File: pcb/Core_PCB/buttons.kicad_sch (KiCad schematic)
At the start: 22 parts, among them J2 Conn_01x08, J8 Conn_01x02_MountingPin, Q1 BSN20, U2 MPR121_BREAKOUT

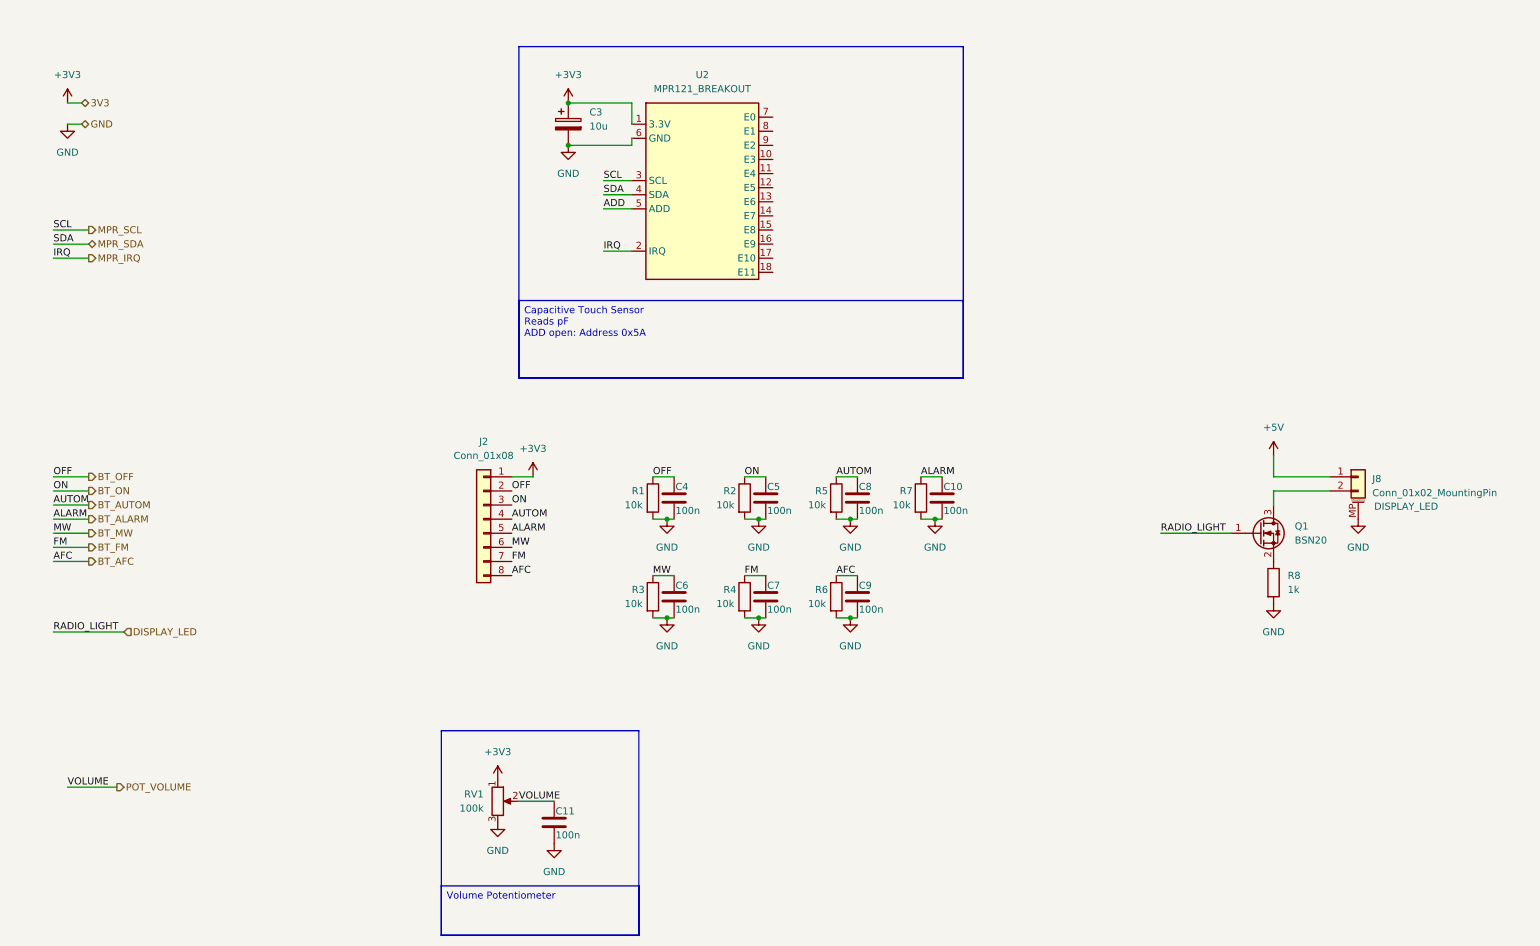
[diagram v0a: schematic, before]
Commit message: SCH: audio gain control via mux (HEF4051), buttons read via i2c io expander (MCP23017)
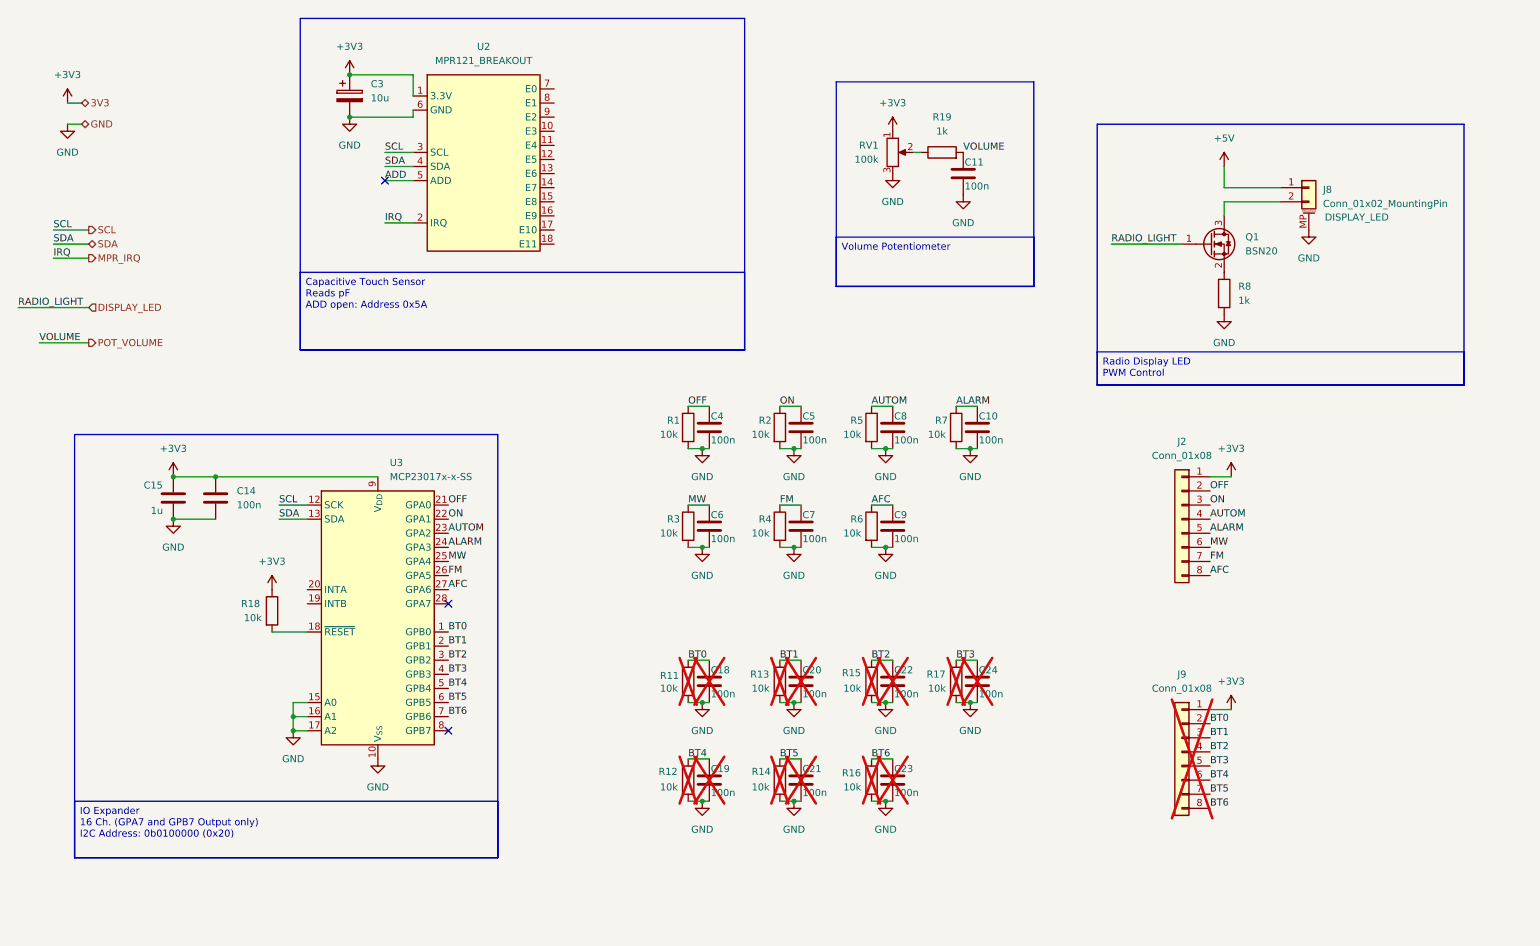
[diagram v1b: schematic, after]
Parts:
- added C14: 100n, symbol Device:C
- added C15: 1u, symbol Device:C
- added C18, C19, C20, C21, C22, C23, C24: 100n, Capacitor_SMD:C_0603_1608Metric_Pad1.08x0.95mm_HandSolder, symbol Device:C
- added J9: Conn_01x08, symbol Connector_Generic:Conn_01x08
- added R11, R12, R13, R14, R15, R16, R17, R18: 10k, Resistor_SMD:R_0603_1608Metric_Pad0.98x0.95mm_HandSolder, symbol Device:R
- added R19: 1k, symbol Device:R
- added U3: MCP23017x-x-SS, Package_SO:SSOP-28_5.3x10.2mm_P0.65mm, symbol Interface_Expansion:MCP23017x-x-SS
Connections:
- net +3V3: now also C14.1, C15.1, J9.1 (Pin_1), R18.1, U3.9 (V_{DD})
- net GND: now also C14.2, C15.2, C18.2, C19.2, C20.2, C21.2, C22.2, C23.2, C24.2, R11.2, R12.2, R13.2, R14.2, R15.2, R16.2, R17.2, U3.10 (V_{SS}), U3.15 (A0), U3.16 (A1), U3.17 (A2)
- net POT_VOLUME: now also R19.2; no longer RV1.2
- net BT_AFC renamed AFC
- net AFC: now also U3.27 (GPA6)
- net BT_ALARM renamed ALARM
- net ALARM: now also U3.24 (GPA3)
- net BT_AUTOM renamed AUTOM
- net AUTOM: now also U3.23 (GPA2)
- net BT_FM renamed FM
- net FM: now also U3.26 (GPA5)
- net BT_MW renamed MW
- net MW: now also U3.25 (GPA4)
- net BT_OFF renamed OFF
- net OFF: now also U3.21 (GPA0)
- net BT_ON renamed ON
- net ON: now also U3.22 (GPA1)
- net MPR_SCL renamed SCL
- net SCL: now also U3.12 (SCK)
- net MPR_SDA renamed SDA
- net SDA: now also U3.13 (SDA)
- new net: R19.1, RV1.2
- new net: R18.2, U3.18 (~{RESET})
- new net BT0: C18.1, J9.2 (Pin_2), R11.1, U3.1 (GPB0)
- new net BT1: C20.1, J9.3 (Pin_3), R13.1, U3.2 (GPB1)
- new net BT2: C22.1, J9.4 (Pin_4), R15.1, U3.3 (GPB2)
- new net BT3: C24.1, J9.5 (Pin_5), R17.1, U3.4 (GPB3)
- new net BT4: C19.1, J9.6 (Pin_6), R12.1, U3.5 (GPB4)
- new net BT5: C21.1, J9.7 (Pin_7), R14.1, U3.6 (GPB5)
- new net BT6: C23.1, J9.8 (Pin_8), R16.1, U3.7 (GPB6)
- no-connect marks 0 -> 3
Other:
- moved on the sheet: C10, C3, C4, C5, C6, C7, C8, C9, J2, J8, Q1, R1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

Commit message: SCH: annotated sheets, reannotated all components
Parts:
- RV1: Name (none) -> VOLUME
- renumbered C5 to C10, C8 to C11, C10 to C12, C15 to C13, C6 to C15, C7 to C16, C9 to C17, C20 to C19, C22 to C20, C24 to C21, C19 to C22, C21 to C23, C23 to C24, C3 to C7, C11 to C8, C4 to C9, J8 to J7, J2 to J8, R4 to R10, R6 to R11, R18 to R12, R11 to R13, R13 to R14, R17 to R16, R12 to R17, R14 to R18, R16 to R19, R19 to R3, R8 to R4, R1 to R5, R2 to R6, R5 to R7, R7 to R8, R3 to R9, U2 to U3, U3 to U4
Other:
- company: (none) -> brunolalb@gmail.com
- title: (none) -> Alarm Clock Resto Mod - Core PCB

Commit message: SCH: assigned footprints to what had missing, replaced some polarized caps with non polarized, added connector for capacitance sensor, ran electric test and fixed minor issues
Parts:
- added J10: Conn_01x12, Connector_PinSocket_2.54mm:PinSocket_1x12_P2.54mm_Vertical, symbol Connector_Generic:Conn_01x12
- C13: footprint (none) -> Capacitor_SMD:C_0805_2012Metric_Pad1.18x1.45mm_HandSolder
- C14: footprint (none) -> Capacitor_SMD:C_0603_1608Metric_Pad1.08x0.95mm_HandSolder
- C7: footprint (none) -> Capacitor_SMD:C_0805_2012Metric_Pad1.18x1.45mm_HandSolder; symbol Device:C_Polarized -> Device:C
- J7: footprint (none) -> RadioWecker:JST_S2B-XH-SM4-TB
- J8, J9: footprint (none) -> Connector_PinSocket_2.54mm:PinSocket_1x08_P2.54mm_Vertical
- R3, R4, RV1: footprint (none) -> Resistor_SMD:R_0603_1608Metric_Pad0.98x0.95mm_HandSolder
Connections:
- net at U3.10 (E3): now also J10.4 (Pin_4)
- net at U3.11 (E4): now also J10.5 (Pin_5)
- net at U3.12 (E5): now also J10.6 (Pin_6)
- net at U3.13 (E6): now also J10.7 (Pin_7)
- net at U3.14 (E7): now also J10.8 (Pin_8)
- net at U3.15 (E8): now also J10.9 (Pin_9)
- net at U3.16 (E9): now also J10.10 (Pin_10)
- net at U3.17 (E10): now also J10.11 (Pin_11)
- net at U3.18 (E11): now also J10.12 (Pin_12)
- net at U3.7 (E0): now also J10.1 (Pin_1)
- net at U3.8 (E1): now also J10.2 (Pin_2)
- net at U3.9 (E2): now also J10.3 (Pin_3)
- net POT_VOLUME renamed VOLUME_POT
- no-connect marks 3 -> 5

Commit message: SCH - audio: screw terminal was facing the wrong direction; buttons: volume pot had wrong footprint, added +5V input; processor: use alternative arduino symbol and custom footprint (with 3d model), added reset switch, adjusted rule for PWR lines
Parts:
- RV1: footprint Resistor_SMD:R_0603_1608Metric_Pad0.98x0.95mm_HandSolder -> Connector_PinSocket_2.54mm:PinSocket_1x03_P2.54mm_Vertical
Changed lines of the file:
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@@
+	(wire
+		(pts
+			(xy 30.48 24.13) (xy 33.02 24.13)
+		)
+		(stroke
+			(width 0)
+			(type default)
+		)
+	)
 	(wire
 		(pts
@@
 			)
 			(justify left bottom)
+		)
+	)
+	(hierarchical_label "+5V"
+		(shape bidirectional)
+		(at 33.02 24.13 0)
+		(effects
+			(font
+				(size 1.27 1.27)
+			)
+			(justify left)
 		)
 	)
@@
 			)
 		)
-		(property "Footprint" "Resistor_SMD:R_0603_1608Metric_Pad0.98x0.95mm_HandSolder"
+		(property "Footprint" "Connector_PinSocket_2.54mm:PinSocket_1x03_P2.54mm_Vertical"
 			(at 179.07 43.18 0)
 			(hide yes)
@@
 					(unit 1)
 				)
+			)
+		)
+	)
+	(symbol
+		(lib_id "power:+5V")
+		(at 30.48 24.13 0)
+		(unit 1)
+		(body_style 1)
+		(exclude_from_sim no)
+		(in_bom yes)
+		(on_board yes)
+		(in_pos_files yes)
+		(dnp no)
+		(fields_autoplaced yes)
+		(property "Reference" "#PWR068"
+			(at 30.48 27.94 0)
+			(hide yes)
+			(show_name no)
+			(do_not_autoplace no)
+			(effects
+				(font
+					(size 1.27 1.27)
+				)
+			)
+		)
+		(property "Value" "+5V"
+			(at 30.48 19.05 0)
+			(show_name no)
+			(do_not_autoplace no)
+			(effects
+				(font
+					(size 1.27 1.27)
+				)
+			)
+		)
+		(property "Footprint" ""
+			(at 30.48 24.13 0)
+			(hide yes)
+			(show_name no)
+			(do_not_autoplace no)
+			(effects
+				(font
+					(size 1.27 1.27)
+				)
+			)
+		)
+		(property "Datasheet" ""
+			(at 30.48 24.13 0)
+			(hide yes)
+			(show_name no)
+			(do_not_autoplace no)
+			(effects
+				(font
+					(size 1.27 1.27)
+				)
+			)
+		)
+		(property "Description" "Power symbol creates a global label with name \"+5V\""
+			(at 30.48 24.13 0)
+			(hide yes)
+			(show_name no)
+			(do_not_autoplace no)
+			(effects
+				(font
+					(size 1.27 1.27)
+				)
+			)
+		)
+		(pin "1"
+		)
+		(instances
+			(project "Core_PCB"
+				(path "/79975d02-cfea-4cc3-8869-9743c86248b2/07ad0869-cb54-450a-945b-05c9495cd42c"
+					(reference "#PWR068")
+					(unit 1)
+				)

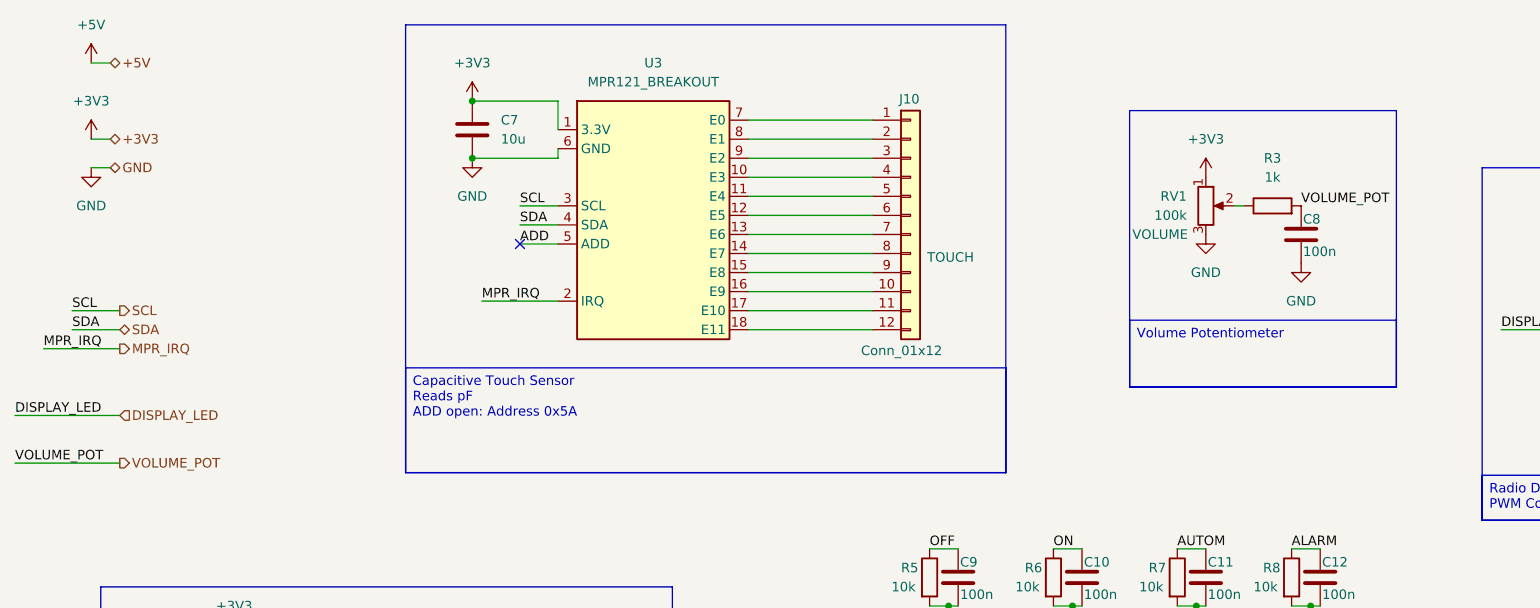
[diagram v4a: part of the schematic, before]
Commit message: use a potentiometer connector (picoblade) and moved it to the audio sch; touch interface (capacitance measureer) got a 2 row connector with GND on one line; added mounting screws and logo to the main sch (and lib)
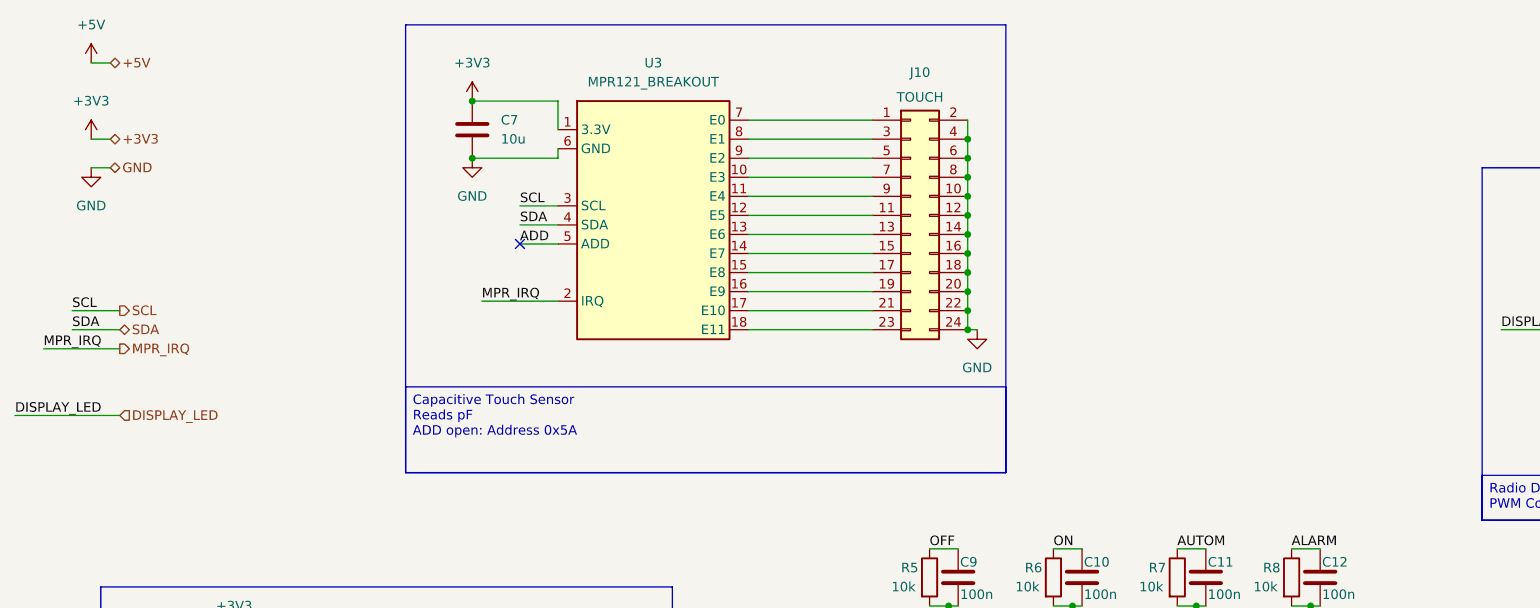
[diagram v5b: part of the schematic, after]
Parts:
- removed C8: 100n, Capacitor_SMD:C_0603_1608Metric_Pad1.08x0.95mm_HandSolder, symbol Device:C
- removed J10: Conn_01x12, Connector_PinSocket_2.54mm:PinSocket_1x12_P2.54mm_Vertical, symbol Connector_Generic:Conn_01x12
- removed R3: 1k, Resistor_SMD:R_0603_1608Metric_Pad0.98x0.95mm_HandSolder, symbol Device:R
- removed RV1: 100k, Connector_PinSocket_2.54mm:PinSocket_1x03_P2.54mm_Vertical, symbol Device:R_Potentiometer
- added J10: Conn_02x12_Odd_Even, Connector_PinSocket_2.54mm:PinSocket_2x12_P2.54mm_Vertical, symbol Connector_Generic:Conn_02x12_Odd_Even
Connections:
- net GND: now also J10.10 (Pin_10), J10.12 (Pin_12), J10.14 (Pin_14), J10.16 (Pin_16), J10.18 (Pin_18), J10.2 (Pin_2), J10.20 (Pin_20), J10.22 (Pin_22), J10.24 (Pin_24), J10.4 (Pin_4), J10.6 (Pin_6), J10.8 (Pin_8)
- net at U3.7 (E0): now also J10.1 (Pin_1)
- net at U3.16 (E9): now also J10.19 (Pin_19)
- net at U3.17 (E10): now also J10.21 (Pin_21)
- net at U3.18 (E11): now also J10.23 (Pin_23)
- net at U3.8 (E1): now also J10.3 (Pin_3)
- net at U3.9 (E2): now also J10.5 (Pin_5)
- net at U3.10 (E3): now also J10.7 (Pin_7)
- net at U3.11 (E4): now also J10.9 (Pin_9)
- net at U3.12 (E5): now also J10.11 (Pin_11)
- net at U3.13 (E6): now also J10.13 (Pin_13)
- net at U3.14 (E7): now also J10.15 (Pin_15)
- net at U3.15 (E8): now also J10.17 (Pin_17)
